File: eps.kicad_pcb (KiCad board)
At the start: 4 copper layers, 95.9 x 90.2 mm, 179 parts, among them J1 PC104-8BIT, J2 PC104PTH, J3 PC104PTH, J4 PC104PTH, J5 PC104PTH, P1 3pin-DC-power, P2 3pin-DC-power, Q10 CSD17551Q3A, Q11 CSD17551Q3A, Q12 CSD17551Q3A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

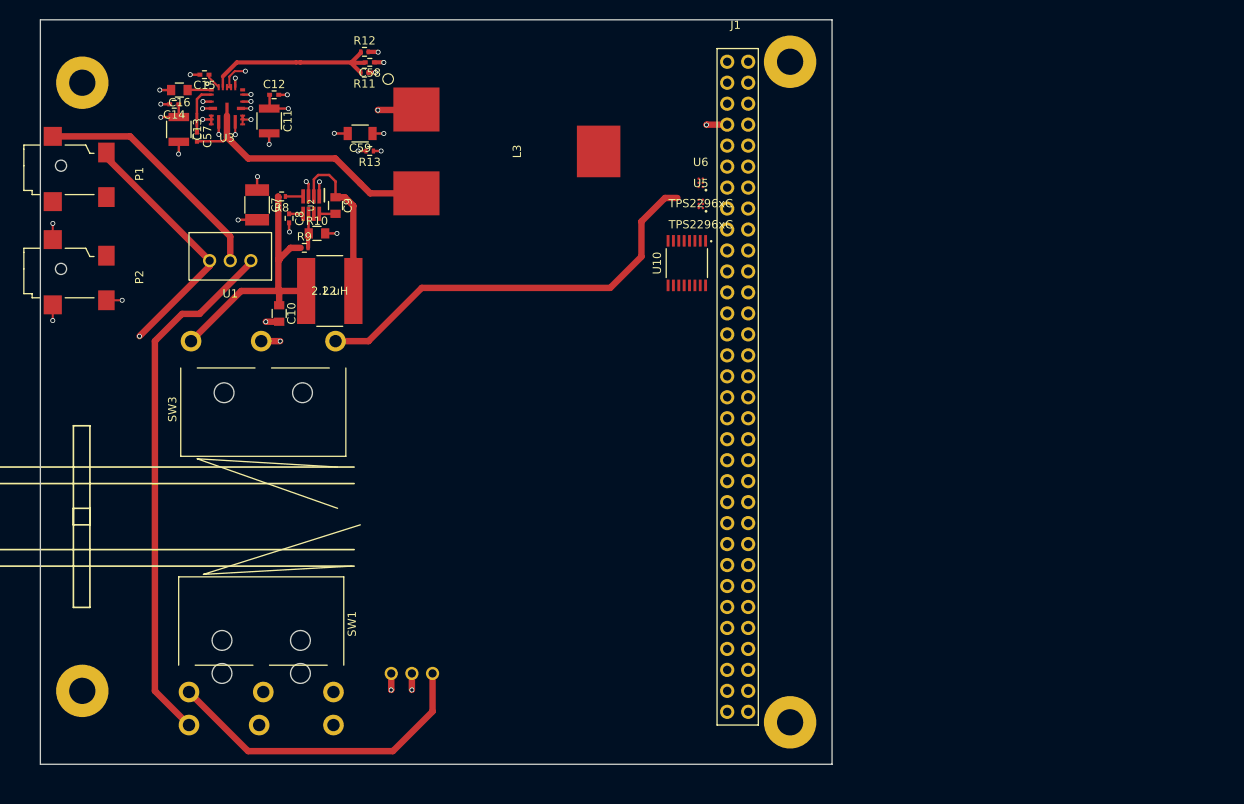
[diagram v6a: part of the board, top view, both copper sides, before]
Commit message: Attempt 2 at laying out 3.3V and 1.6A PD
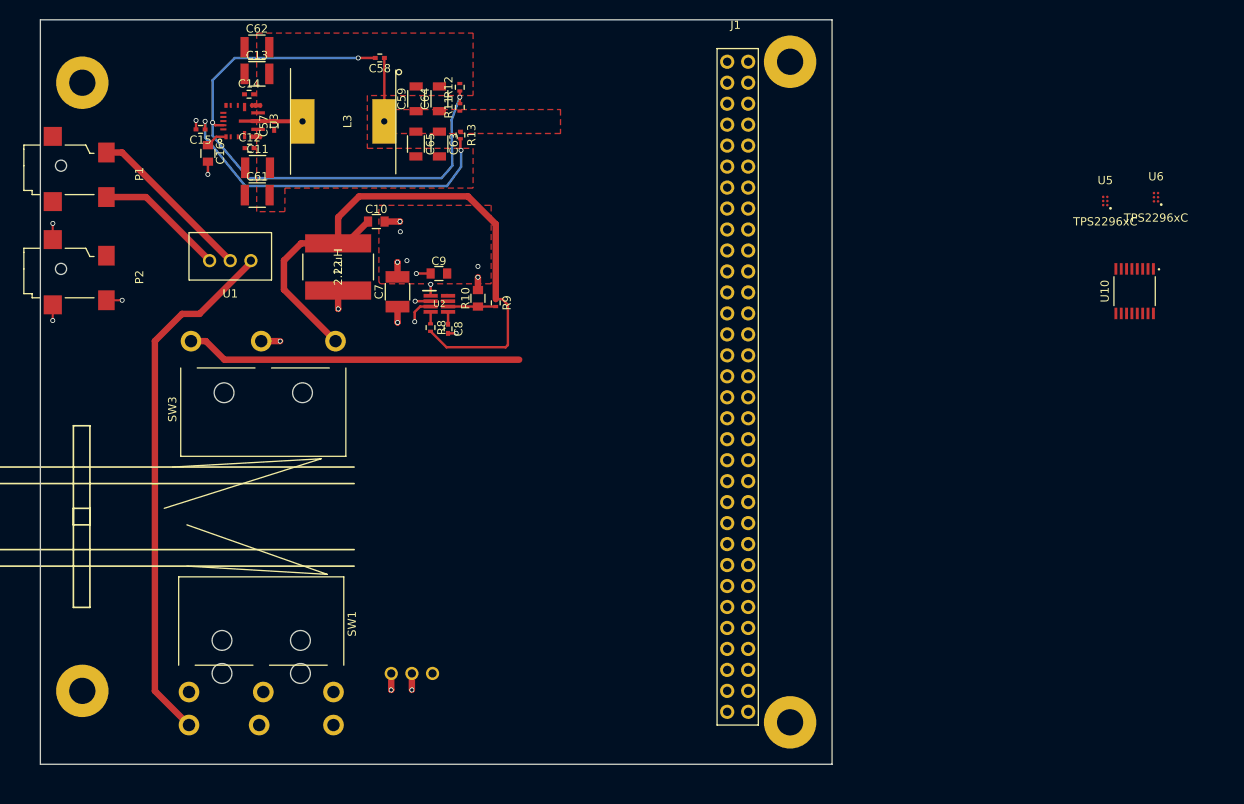
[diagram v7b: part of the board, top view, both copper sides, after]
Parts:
- added C61: 10.0 uF, Capacitors_SMD:C_1210, F.Cu at (131.3, 66.1)
- added C62: 10.0 uF, Capacitors_SMD:C_1210, F.Cu at (131.2, 48.2)
- added C63: 68.0 uF, Capacitors_SMD:C_1206, F.Cu at (153.3, 59.9)
- added C64: 68.0 uF, Capacitors_SMD:C_1206, F.Cu at (153.3, 54.4)
- added C65: 68.0 uF, Capacitors_SMD:C_1206, F.Cu at (150.5, 59.9)
- L3: footprint SFUSat-ind:SER2915L-103KL -> SFUSat-ind:L_7447709100
- SW1: footprint SFUSat:SS-3GLPD-R -> SFUSat:SS-3GLPD-L
- SW3: footprint SFUSat:SS-3GLPD-L -> SFUSat:SS-3GLPD-R
- moved U6 55.2 mm to (240.1, 66.3)
- moved U10 54.3 mm to (237.5, 77.7)
- moved U5 49.0 mm to (234.0, 66.8)
- moved R9 24.1 mm to (160.2, 79.1), turned to 270 degrees
- moved R8 24.0 mm to (152.3, 82.1), turned to 270 degrees
- moved L3 23.5 mm to (141.7, 57.1), turned to 90 degrees
- moved C8 23.4 mm to (154.4, 82.3)
- moved R10 21.0 mm to (158.0, 78.6), turned to 90 degrees
- moved C7 20.0 mm to (148.3, 77.8), turned to 90 degrees
- moved U2 19.6 mm to (153.3, 79.2), turned to 0 degrees
- moved C10 16.2 mm to (145.7, 69.3), turned to 0 degrees
- moved C9 15.0 mm to (153.3, 75.6), turned to 0 degrees
- moved R12 12.3 mm to (155.8, 53.0), turned to 90 degrees
- moved R11 12.3 mm to (155.8, 55.4), turned to 90 degrees
- moved C13 11.6 mm to (131.2, 51.4), turned to 0 degrees
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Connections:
- C14 pad 2: GND -> Net-(C14-Pad2)
- R13 pad 2: GND -> Net-(C15-Pad1)
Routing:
- net Net-(C58-Pad2): track 22.9 -> 71.1 mm, vias 0 -> 3
- net /1.6A_Regulator_PDB/1.6A: track 33.6 -> 75.2 mm
- net Net-(C15-Pad1): track 2.00 -> 41.3 mm, vias 0 -> 2
- net /Vin_Solar: track 39.1 -> 0.00 mm
- net Net-(C57-Pad2): track 34.8 -> 6.15 mm
- net GND: track 39.7 -> 18.1 mm, vias 24 -> 10
- net Net-(C9-Pad1): track 20.1 -> 5.85 mm, vias 0 -> 3
- net /pack-: track 29.4 -> 15.7 mm
- net /VSYS_RETURN: track 15.9 -> 5.30 mm, vias 8 -> 2
- net /PowerDistributionDeploymentControl/1.6A: track 51.1 -> 40.7 mm
- net /pack+: track 30.9 -> 21.0 mm, vias 1 -> 0
- net Net-(C57-Pad1): track 7.54 -> 0.00 mm
- net /3V3: track 11.0 -> 7.69 mm, vias 6 -> 0
- net Net-(C9-Pad2): track 1.98 -> 0.16 mm
- net Net-(R10-Pad1): track 4.14 -> 5.78 mm
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- added copper zone on F.Cu, net /3V3
- added copper zone on F.Cu, net GND
- added copper zone on PWR.Cu, net Net-(C9-Pad2)
- removed copper zone on PWR.Cu, net /3V3

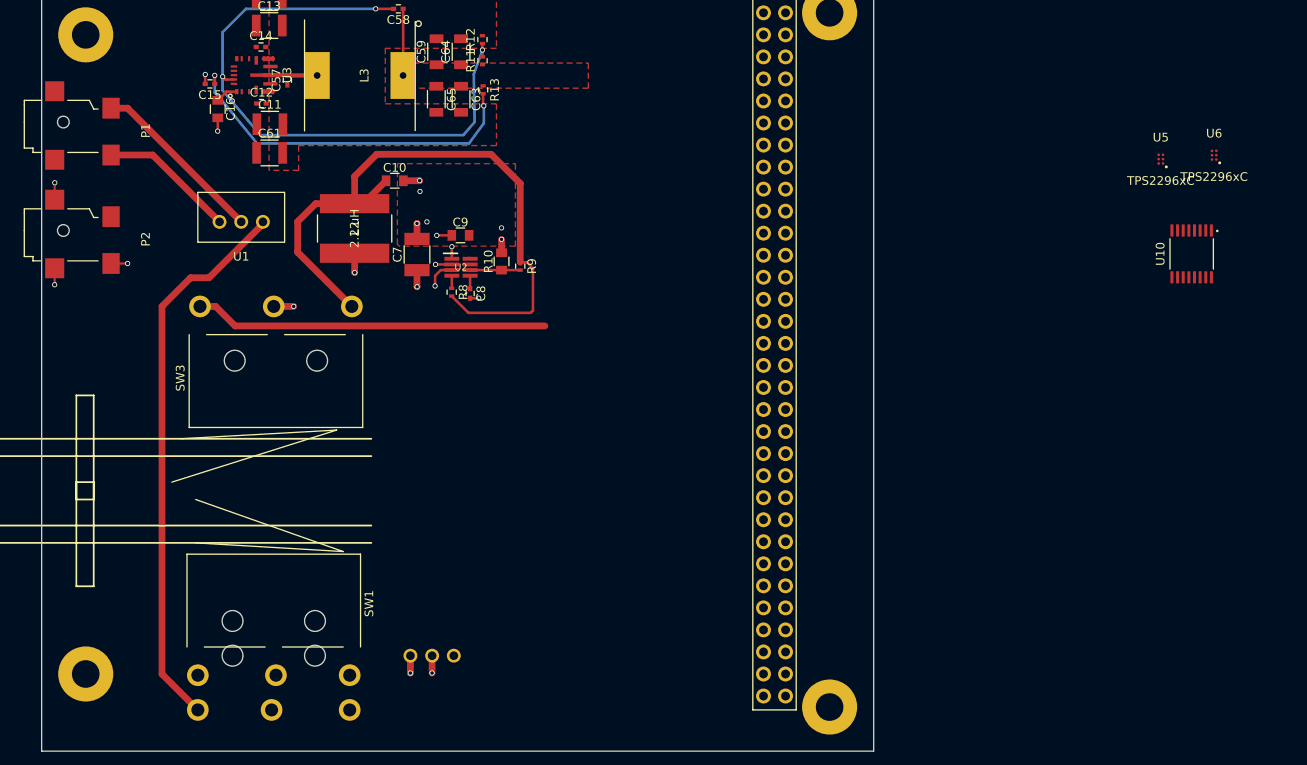
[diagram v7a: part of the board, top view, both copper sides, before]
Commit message: Updated GND Layer
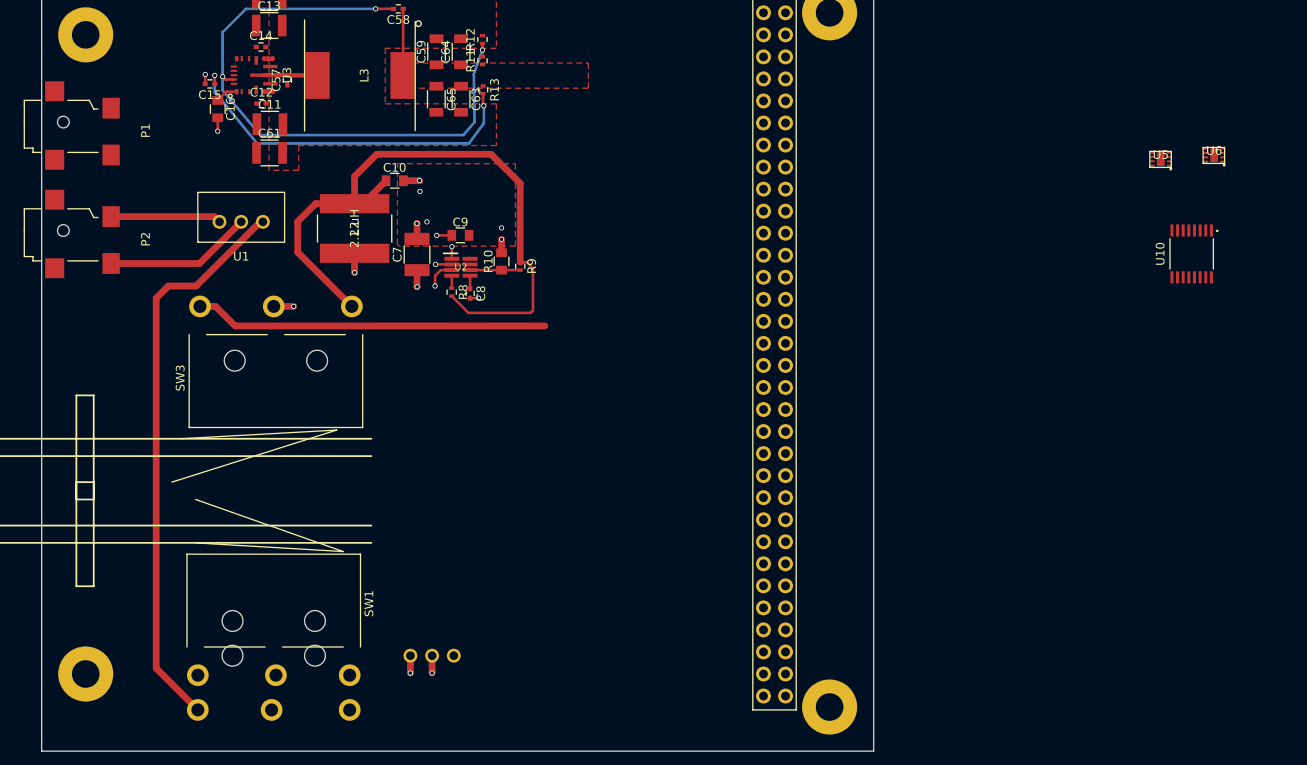
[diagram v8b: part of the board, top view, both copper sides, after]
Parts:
- U5, U6: footprint SFUSat:TPS22964CYZPR -> SFUSat:TPS22967
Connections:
- P1 pad 1: /pack+ -> /VSYS_RETURN
- P1 pad 2: /pack- -> GND
- P1 pad 3: /pack- -> GND
- P2 pad 1: /VSYS_RETURN -> /pack+
- P2 pad 2: GND -> /pack-
- P2 pad 3: GND -> /pack-
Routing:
- net /pack+: track 21.0 -> 12.7 mm
- net GND: track 18.1 -> 12.3 mm, vias 10 -> 7
- net /return: track 64.0 -> 65.6 mm
- net /pack-: track 15.7 -> 17.0 mm
- net /VSYS_RETURN: track 5.30 -> 5.90 mm
- added copper zone on GND.Cu, net GND
